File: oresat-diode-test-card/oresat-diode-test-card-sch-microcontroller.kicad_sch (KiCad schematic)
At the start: 25 parts, among them J7 ORESAT-DEBUG-CONNECTOR-ALL, U1 TCAN330, U7 STM32F091C, X2 CRYSTAL-WITH-GND

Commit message: added actual files
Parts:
- removed JP11, JP8: PINHD-2X10, oresat-proto-card:2X10, symbol oresat-proto-card-eagle-import:PINHD-2X10
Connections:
- no-connect marks 6 -> 4

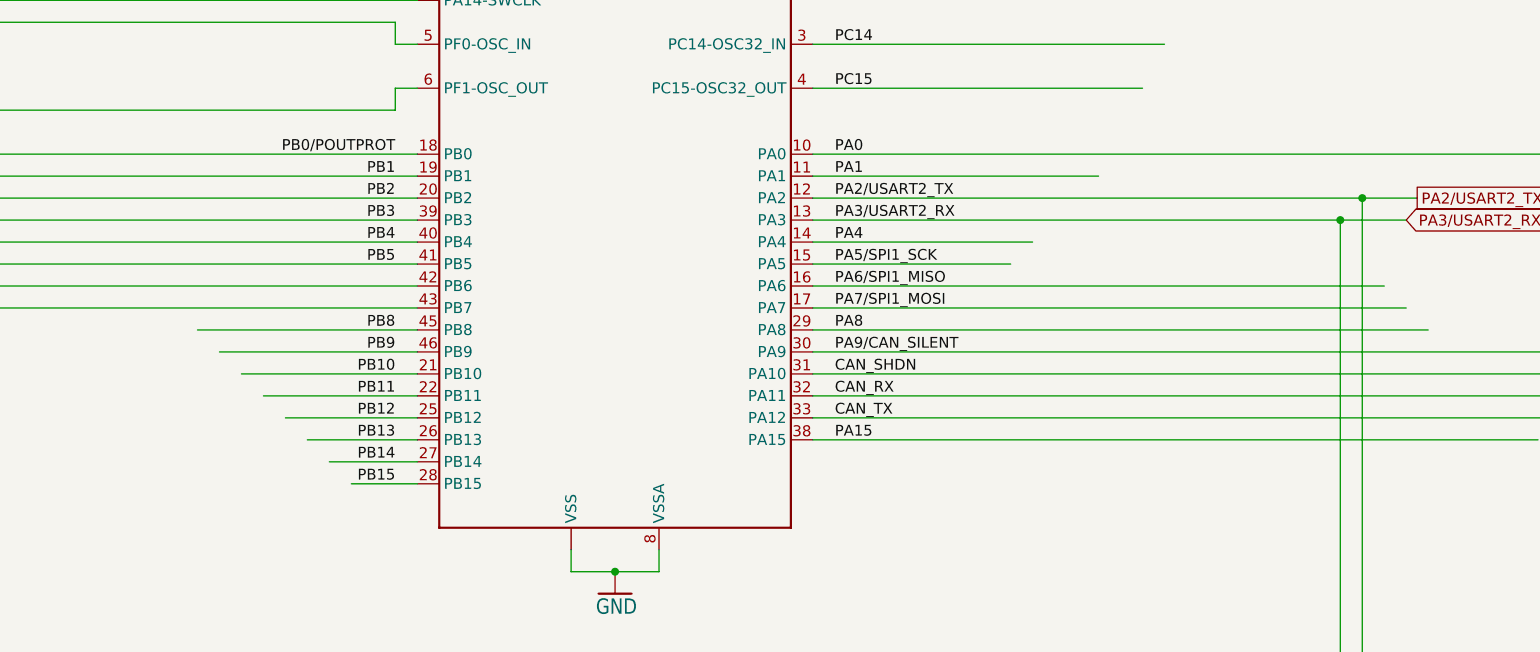
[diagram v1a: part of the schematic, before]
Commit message: Quick design review on schematic; basically ready for layout.
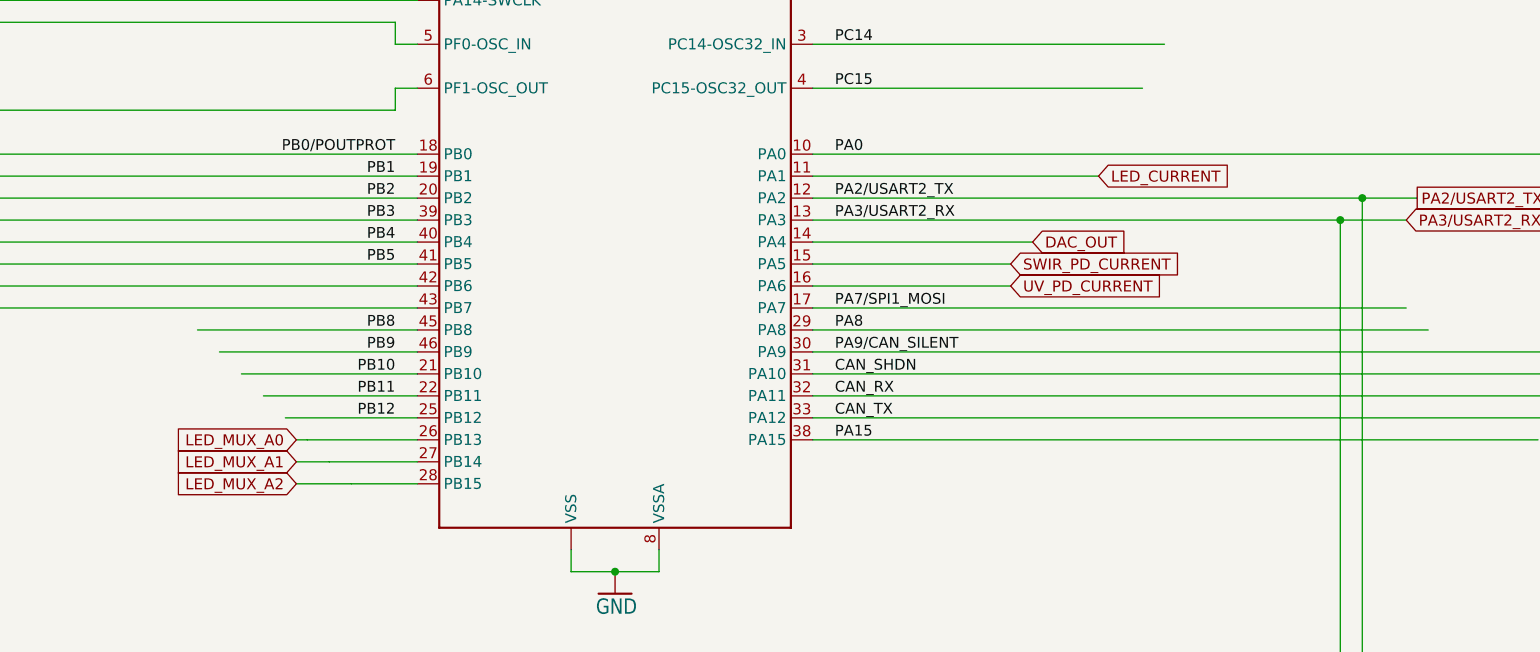
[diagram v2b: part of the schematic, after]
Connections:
- net PA1 renamed LED_CURRENT
- net PA4 renamed DAC_OUT
- net PA5/SPI1_SCK renamed SWIR_PD_CURRENT
- net PA6/SPI1_MISO renamed UV_PD_CURRENT
- net PB13 renamed LED_MUX_A0
- net PB14 renamed LED_MUX_A1
- net PB15 renamed LED_MUX_A2
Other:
- title: OreSat M0 Proto Card: Microcontroller -> OreSat Diode Test Card
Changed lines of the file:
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@@
 	(paper "USLedger")
 	(title_block
-		(title "OreSat M0 Proto Card: Microcontroller")
-		(date "2024-03-21")
-		(rev "5.0")
+		(title "OreSat Diode Test Card")
+		(date "2024-04-21")
+		(rev "v1.0")
 	)
 	(junction
@@
 	(wire
 		(pts
+			(xy 186.69 118.11) (xy 193.04 118.11)
+		)
+		(stroke
+			(width 0)
+			(type default)
+		)
+	)
+	(wire
+		(pts
 			(xy 365.76 102.87) (xy 365.76 107.95)
 		)
@@
 	(wire
 		(pts
+			(xy 186.69 113.03) (xy 187.96 113.03)
+		)
+		(stroke
+			(width 0)
+			(type default)
+		)
+	)
+	(wire
+		(pts
 			(xy 370.84 102.87) (xy 365.76 102.87)
 		)
@@
 	(wire
 		(pts
-			(xy 246.38 95.25) (xy 312.42 95.25)
-		)
-		(stroke
-			(width 0.1524)
-			(type solid)
-		)
-	)
-	(wire
-		(pts
 			(xy 38.1 207.01) (xy 41.91 207.01)
 		)
@@
 	(wire
 		(pts
+			(xy 186.69 115.57) (xy 190.5 115.57)
+		)
+		(stroke
+			(width 0)
+			(type default)
+		)
+	)
+	(wire
+		(pts
 			(xy 215.9 21.59) (xy 220.98 21.59)
 		)
@@
 	(wire
 		(pts
+			(xy 246.38 95.25) (xy 269.24 95.25)
+		)
+		(stroke
+			(width 0)
+			(type default)
+		)
+	)
+	(wire
+		(pts
 			(xy 53.34 214.63) (xy 38.1 214.63)
 		)
@@
 		)
 	)
-	(label "PB14"
-		(at 198.12 115.57 180)
-		(fields_autoplaced yes)
-		(effects
-			(font
-				(size 1.2446 1.2446)
-			)
-			(justify right bottom)
-		)
-	)
 	(label "CAN_SHDN"
 		(at 248.92 105.41 0)
@@
 		)
 	)
-	(label "PB15"
-		(at 198.12 118.11 180)
-		(fields_autoplaced yes)
-		(effects
-			(font
-				(size 1.2446 1.2446)
-			)
-			(justify right bottom)
-		)
-	)
 	(label "NRESET"
 		(at 40.64 171.45 0)
@@
 		)
 	)
-	(label "PA5/SPI1_SCK"
-		(at 248.92 92.71 0)
-		(fields_autoplaced yes)
-		(effects
-			(font
-				(size 1.2446 1.2446)
-			)
-			(justify left bottom)
-		)
-	)
 	(label "PA9/CAN_SILENT"
 		(at 248.92 102.87 0)
@@
 		)
 	)
-	(label "PA1"
-		(at 248.92 82.55 0)
-		(fields_autoplaced yes)
-		(effects
-			(font
-				(size 1.2446 1.2446)
-			)
-			(justify left bottom)
-		)
-	)
-	(label "PA4"
-		(at 248.92 90.17 0)
-		(fields_autoplaced yes)
-		(effects
-			(font
-				(size 1.2446 1.2446)
-			)
-			(justify left bottom)
-		)
-	)
 	(label "BOOT0"
 		(at 198.12 57.15 180)
@@
 		)
 	)
-	(label "PB13"
-		(at 198.12 113.03 180)
-		(fields_autoplaced yes)
-		(effects
-			(font
-				(size 1.2446 1.2446)
-			)
-			(justify right bottom)
-		)
-	)
 	(label "PB2"
 		(at 198.12 85.09 180)
@@
 		)
 	)
-	(label "PA6/SPI1_MISO"
-		(at 248.92 95.25 0)
-		(fields_autoplaced yes)
-		(effects
-			(font
-				(size 1.2446 1.2446)
-			)
-			(justify left bottom)
-		)
-	)
 	(label "PA3/USART2_RX"
 		(at 40.64 186.69 0)
@@
 					(size 1.27 1.27)
 				)
+				(justify right)
+			)
+		)
+	)
+	(global_label "LED_CURRENT"
+		(shape input)
+		(at 279.4 82.55 0)
+		(fields_autoplaced yes)
+		(effects
+			(font
+				(size 1.27 1.27)
+			)
+			(justify left)
+		)
+		(property "Intersheetrefs" "${INTERSHEET_REFS}"
+			(at 295.3875 82.55 0)
+			(effects
+				(font
+					(size 1.27 1.27)
+				)
+				(justify left)
+			)
+		)
+	)
+	(global_label "LED_MUX_A1"
+		(shape input)
+		(at 186.69 115.57 180)
+		(fields_autoplaced yes)
+		(effects
+			(font
+				(size 1.27 1.27)
+			)
+			(justify right)
+		)
+		(property "Intersheetrefs" "${INTERSHEET_REFS}"
+			(at 172.033 115.57 0)
+			(effects
+				(font
+					(size 1.27 1.27)
+				)
+				(justify right)
+			)
+		)
+	)
+	(global_label "DAC_OUT"
+		(shape input)
+		(at 271.78 90.17 0)
+		(fields_autoplaced yes)
+		(effects
+			(font
+				(size 1.27 1.27)
+			)
+			(justify left)
+		)
+		(property "Intersheetrefs" "${INTERSHEET_REFS}"
+			(at 282.99 90.17 0)
+			(effects
+				(font
+					(size 1.27 1.27)
+				)
 				(justify left)
 			)
@@
 		)
 	)
+	(global_label "SWIR_PD_CURRENT"
+		(shape input)
+		(at 269.24 92.71 0)
+		(fields_autoplaced yes)
+		(effects
+			(font
+				(size 1.27 1.27)
+			)
+			(justify left)
+		)
+		(property "Intersheetrefs" "${INTERSHEET_REFS}"
+			(at 289.8237 92.71 0)
+			(effects
+				(font
+					(size 1.27 1.27)
+				)
+				(justify left)
+			)
+		)
+	)
 	(global_label "CAN2_H"
 		(shape bidirectional)
@@
 		)
 	)
+	(global_label "UV_PD_CURRENT"
+		(shape input)
+		(at 269.24 95.25 0)
+		(fields_autoplaced yes)
+		(effects
+			(font
+				(size 1.27 1.27)
+			)
+			(justify left)
+		)
+		(property "Intersheetrefs" "${INTERSHEET_REFS}"
+			(at 287.7071 95.25 0)
+			(effects
+				(font
+					(size 1.27 1.27)
+				)
+				(justify left)
+			)
+		)
+	)
+	(global_label "LED_MUX_A0"
+		(shape input)
+		(at 186.69 113.03 180)
+		(fields_autoplaced yes)
+		(effects
+			(font
+				(size 1.27 1.27)
+			)
+			(justify right)
+		)
+		(property "Intersheetrefs" "${INTERSHEET_REFS}"
+			(at 172.033 113.03 0)
+			(effects
+				(font
+					(size 1.27 1.27)
+				)
+				(justify right)
+			)
+		)
+	)
+	(global_label "LED_MUX_A2"
+		(shape input)
+		(at 186.69 118.11 180)
+		(fields_autoplaced yes)
+		(effects
+			(font
+				(size 1.27 1.27)
+			)
+			(justify right)
+		)
+		(property "Intersheetrefs" "${INTERSHEET_REFS}"
+			(at 172.033 118.11 0)
+			(effects
+				(font
+					(size 1.27 1.27)
+				)
+				(justify right)
+			)
+		)
+	)
 	(global_label "BOOT0"
 		(shape bidirectional)
@@
 			)
 		)
-		(property "Datasheet" ""
+		(property "Datasheet" "https://www.st.com/content/ccc/resource/technical/document/datasheet/95/3c/2e/5b/21/09/45/a6/DM00115237.pdf/files/DM00115237.pdf/jcr:content/translations/en.DM00115237.pdf"
 			(at 223.52 85.09 0)
 			(effects

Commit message: Lots of schematic cleanup - replace weird ground and power symbols with more kicad ones, fix values, fix OPD connections and address, update PCB
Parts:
- removed R50, R51: 4.7k, oresat-passives:0603-C-NOSILK, symbol oresat-proto-card-eagle-import:R-US_0603-C-NOSILK
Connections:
- net PA15: no longer names the net of U7.38 (PA15)
- net PA7/SPI1_MOSI: no longer names the net of U7.17 (PA7)
- net PA8: no longer names the net of U7.29 (PA8)
- net PB1: no longer names the net of U7.19 (PB1)
- net PB10: no longer names the net of U7.21 (PB10)
- net PB11: no longer names the net of U7.22 (PB11)
- net PB12 renamed ~{LED_MUX_ENABLE}
- net PB2: no longer names the net of U7.20 (PB2)
- net PB3: no longer names the net of U7.39 (PB3)
- net PB4: no longer names the net of U7.40 (PB4)
- net PB5: no longer names the net of U7.41 (PB5)
- net PB6/SCL: no longer names the net of U7.42 (PB6)
- net PB7/SDA: no longer names the net of U7.43 (PB7)
- net PB8: no longer names the net of U7.45 (PB8)
- net PB9: no longer names the net of U7.46 (PB9)
- net PC13: no longer names the net of U7.2 (PC13)
- net PC14: no longer names the net of U7.3 (PC14-OSC32_IN)
- net PC15: no longer names the net of U7.4 (PC15-OSC32_OUT)
- no-connect marks 4 -> 21
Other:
- note removed: "Emergency M0 bootstrapping over OPD I2C Address: 0b0111110x"
- moved on the sheet: C13, C14, C15, C18, C19, C20, C21, D5, R47, R48, R49, TP25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

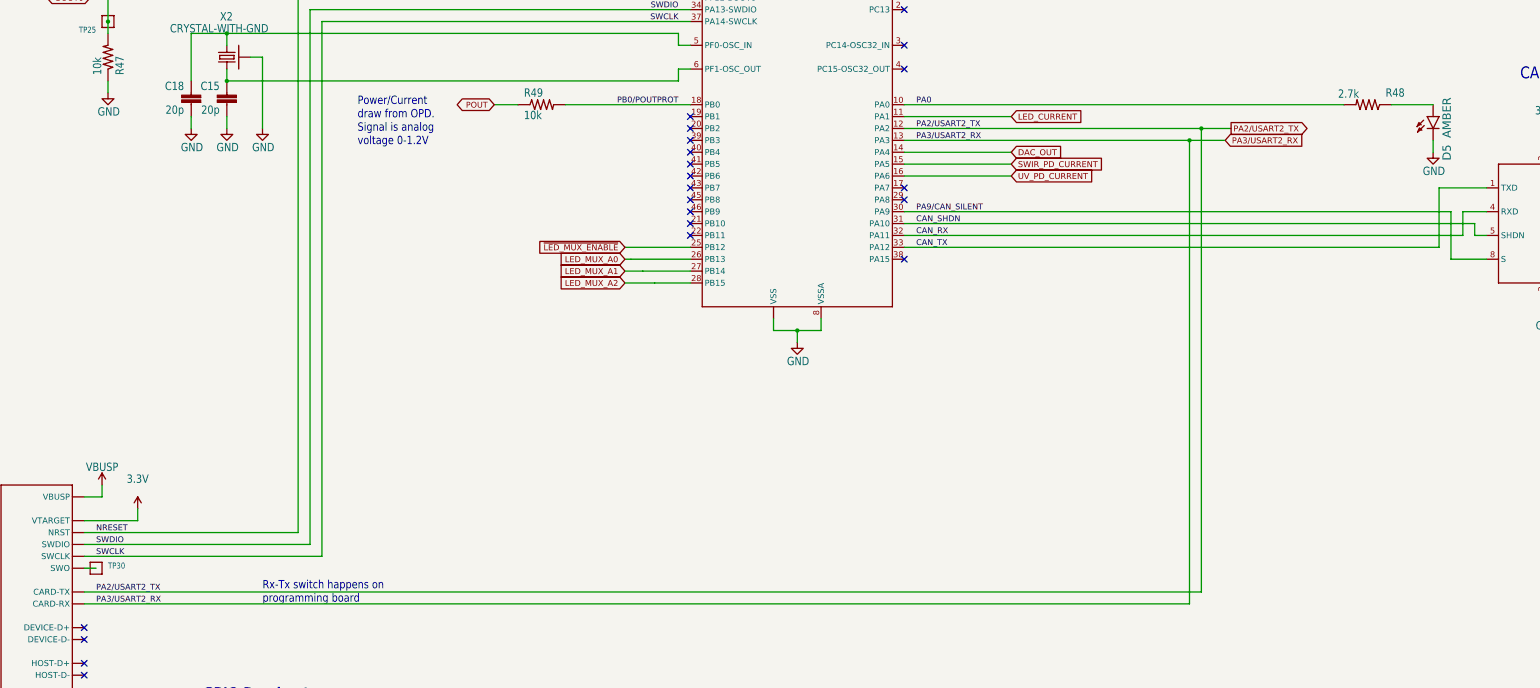
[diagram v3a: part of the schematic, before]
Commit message: Clean up of EAGLE imported ICs, added build directory, moved and locked diode hats.
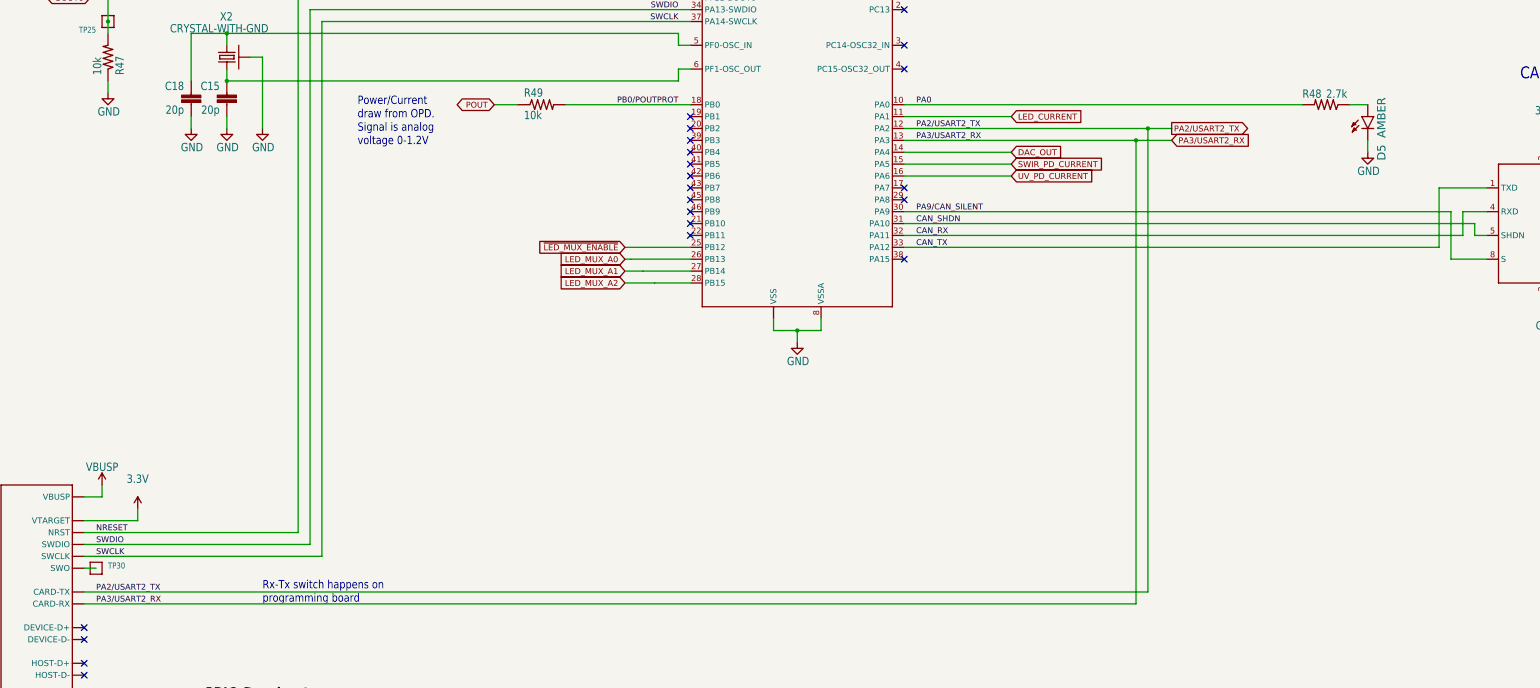
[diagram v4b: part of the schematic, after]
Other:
- moved on the sheet: D5, R48
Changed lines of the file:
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@@
 	)
 	(junction
-		(at 298.45 97.79)
+		(at 287.02 97.79)
 		(diameter 0)
 		(color 0 0 0 0)
 	)
 	(junction
-		(at 300.99 95.25)
+		(at 222.25 31.75)
 		(diameter 0)
 		(color 0 0 0 0)
 	)
 	(junction
-		(at 222.25 31.75)
+		(at 63.5 238.76)
 		(diameter 0)
 		(color 0 0 0 0)
 	)
 	(junction
-		(at 63.5 238.76)
+		(at 212.09 31.75)
 		(diameter 0)
 		(color 0 0 0 0)
 	)
 	(junction
-		(at 212.09 31.75)
+		(at 289.56 95.25)
 		(diameter 0)
 		(color 0 0 0 0)
@@
 	(wire
 		(pts
+			(xy 287.02 97.79) (xy 294.64 97.79)
+		)
+		(stroke
+			(width 0.1524)
+			(type solid)
+		)
+	)
+	(wire
+		(pts
 			(xy 177.8 128.27) (xy 184.15 128.27)
 		)
@@
 	(wire
 		(pts
-			(xy 298.45 196.85) (xy 62.23 196.85)
+			(xy 287.02 196.85) (xy 62.23 196.85)
 		)
 		(stroke
@@
 	(wire
 		(pts
-			(xy 298.45 97.79) (xy 298.45 196.85)
+			(xy 287.02 97.79) (xy 287.02 196.85)
 		)
 		(stroke
@@
 	(wire
 		(pts
-			(xy 237.49 97.79) (xy 298.45 97.79)
-		)
-		(stroke
-			(width 0.1524)
-			(type solid)
-		)
-	)
-	(wire
-		(pts
-			(xy 298.45 97.79) (xy 306.07 97.79)
+			(xy 237.49 97.79) (xy 287.02 97.79)
 		)
 		(stroke
@@
 	(wire
 		(pts
-			(xy 300.99 95.25) (xy 300.99 194.31)
-		)
-		(stroke
-			(width 0.1524)
-			(type solid)
-		)
-	)
-	(wire
-		(pts
-			(xy 300.99 95.25) (xy 307.34 95.25)
+			(xy 289.56 95.25) (xy 289.56 194.31)
 		)
 		(stroke
@@
 	(wire
 		(pts
-			(xy 237.49 90.17) (xy 331.47 90.17)
+			(xy 237.49 90.17) (xy 322.58 90.17)
 		)
 		(stroke
@@
 	(wire
 		(pts
-			(xy 237.49 95.25) (xy 300.99 95.25)
+			(xy 237.49 95.25) (xy 289.56 95.25)
 		)
 		(stroke
@@
 	(wire
 		(pts
-			(xy 350.52 97.79) (xy 350.52 100.33)
+			(xy 336.55 97.79) (xy 336.55 100.33)
 		)
 		(stroke
@@
 	(wire
 		(pts
-			(xy 300.99 194.31) (xy 62.23 194.31)
+			(xy 289.56 194.31) (xy 62.23 194.31)
 		)
 		(stroke
@@
 	(wire
 		(pts
+			(xy 289.56 95.25) (xy 294.64 95.25)
+		)
+		(stroke
+			(width 0.1524)
+			(type solid)
+		)
+	)
+	(wire
+		(pts
 			(xy 222.25 31.75) (xy 227.33 31.75)
 		)
@@
 	(wire
 		(pts
-			(xy 341.63 90.17) (xy 350.52 90.17)
+			(xy 332.74 90.17) (xy 336.55 90.17)
 		)
 		(stroke
@@
 	(global_label "PA2{slash}USART2_TX"
 		(shape output)
-		(at 307.34 95.25 0)
+		(at 294.64 95.25 0)
 		(fields_autoplaced yes)
 		(effects
@@
 		)
 		(property "Intersheetrefs" "${INTERSHEET_REFS}"
-			(at 325.3648 95.25 0)
+			(at 312.6648 95.25 0)
 			(effects
 				(font
@@
 		)
 	)
-	(global_label "PA3{slash}USART2_RX"
+	(global_label "LED_CURRENT"
 		(shape input)
-		(at 306.07 97.79 0)
+		(at 260.35 92.71 0)
+		(fields_autoplaced yes)
 		(effects
 			(font
@@
 		)
 		(property "Intersheetrefs" "${INTERSHEET_REFS}"
-			(at 307.3945 97.7106 0)
+			(at 276.3375 92.71 0)
 			(effects
 				(font
 					(size 1.27 1.27)
 				)
-				(justify right)
+				(justify left)
 			)
 		)
 	)
-	(global_label "LED_CURRENT"
+	(global_label "~{LED_MUX_ENABLE}"
 		(shape input)
-		(at 260.35 92.71 0)
+		(at 177.8 120.65 180)
 		(fields_autoplaced yes)
 		(effects
@@
 				(size 1.27 1.27)
 			)
-			(justify left)
+			(justify right)
 		)
 		(property "Intersheetrefs" "${INTERSHEET_REFS}"
-			(at 276.3375 92.71 0)
+			(at 158.4259 120.65 0)
 			(effects
 				(font
 					(size 1.27 1.27)
 				)
-				(justify left)
+				(justify right)
 			)
 		)
 	)
-	(global_label "~{LED_MUX_ENABLE}"
+	(global_label "PA3{slash}USART2_RX"
 		(shape input)
-		(at 177.8 120.65 180)
+		(at 294.64 97.79 0)
 		(fields_autoplaced yes)
 		(effects
@@
 				(size 1.27 1.27)
 			)
-			(justify right)
+			(justify left)
 		)
 		(property "Intersheetrefs" "${INTERSHEET_REFS}"
-			(at 158.4259 120.65 0)
+			(at 313.0466 97.79 0)
 			(effects
 				(font
 					(size 1.27 1.27)
 				)
-				(justify right)
+				(justify left)
 			)
 		)
@@
 	(symbol
 		(lib_id "oresat-proto-card-eagle-import:R-US_0603-C-NOSILK")
-		(at 336.55 90.17 180)
+		(at 327.66 90.17 180)
 		(unit 1)
 		(exclude_from_sim no)
@@
 		(dnp no)
 		(property "Reference" "R48"
-			(at 340.36 88.6714 0)
+			(at 322.58 88.9 0)
 			(effects
 				(font
@@
 		)
 		(property "Value" "2.7k"
-			(at 330.2 88.9 0)
+			(at 327.66 88.9 0)
 			(effects
 				(font
@@
 		)
 		(property "Footprint" "oresat-passives:0603-C-NOSILK"
-			(at 336.55 90.17 0)
+			(at 327.66 90.17 0)
 			(effects
 				(font
@@
 		)
 		(property "Datasheet" ""
-			(at 336.55 90.17 0)
+			(at 327.66 90.17 0)
 			(effects
 				(font
@@
 		)
 		(property "Description" ""
-			(at 336.55 90.17 0)
+			(at 327.66 90.17 0)
 			(effects
 				(font
@@
 		)
 		(property "DIS" "Digi-Key"
-			(at 336.55 90.17 0)
+			(at 327.66 90.17 0)
 			(effects
 				(font
@@
 		)
 		(property "DPN" "A129632CT-ND"
-			(at 336.55 90.17 0)
+			(at 327.66 90.17 0)
 			(effects
 				(font
@@
 		)
 		(property "MFR" "TE Connectivity"
-			(at 336.55 90.17 0)
+			(at 327.66 90.17 0)
 			(effects
 				(font
@@
 		)
 		(property "MPN" "CRGCQ0402F2K7"
-			(at 336.55 90.17 0)
+			(at 327.66 90.17 0)
 			(effects
 				(font
@@
 	(symbol
 		(lib_id "oresat-proto-card-eagle-import:LED-GREEN0603")
-		(at 350.52 92.71 0)
+		(at 336.55 92.71 0)
 		(unit 1)
 		(exclude_from_sim no)
@@
 		(dnp no)
 		(property "Reference" "D5"
-			(at 352.425 102.108 90)
+			(at 338.455 102.108 90)
 			(effects
 				(font
@@
 		)
 		(property "Value" "AMBER"
-			(at 352.425 97.282 90)
+			(at 338.455 97.282 90)
 			(effects
 				(font
@@
 		)
 		(property "Footprint" "oresat-proto-card:LED-0603"
-			(at 350.52 92.71 0)
+			(at 336.55 92.71 0)
 			(effects
 				(font
@@
 		)
 		(property "Datasheet" ""
-			(at 350.52 92.71 0)
+			(at 336.55 92.71 0)
 			(effects
 				(font
@@
 		)
 		(property "Description" ""
-			(at 350.52 92.71 0)
+			(at 336.55 92.71 0)
 			(effects
 				(font
@@
 		)
 		(property "DIS" "Digi-Key"
-			(at 350.52 92.71 0)
+			(at 336.55 92.71 0)
 			(effects
 				(font
@@
 		)
 		(property "DPN" "1830-1064-1-ND"
-			(at 350.52 92.71 0)
+			(at 336.55 92.71 0)
 			(effects
 				(font
@@
 		)
 		(property "MFR" "Inolux"
-			(at 350.52 92.71 0)
+			(at 336.55 92.71 0)
 			(effects
 				(font
@@
 		)
 		(property "MPN" "IN-S63AT5A"
-			(at 350.52 92.71 0)
+			(at 336.55 92.71 0)
 			(effects
 				(font
@@
 	(symbol
 		(lib_id "power:GND")
-		(at 350.52 100.33 0)
+		(at 336.55 100.33 0)
 		(mirror y)
 		(unit 1)
@@
 		(dnp no)
 		(property "Reference" "#GND062"
-			(at 350.52 100.33 0)
+			(at 336.55 100.33 0)
 			(effects
 				(font
@@
 		)
 		(property "Value" "GND"
-			(at 353.06 105.41 0)
+			(at 339.09 105.41 0)
 			(effects
 				(font
@@
 		)
 		(property "Footprint" ""
-			(at 350.52 100.33 0)
+			(at 336.55 100.33 0)
 			(effects
 				(font
@@
 		)
 		(property "Datasheet" ""
-			(at 350.52 100.33 0)
+			(at 336.55 100.33 0)
 			(effects
 				(font
@@
 		)
 		(property "Description" "Power symbol creates a global label with name \"GND\" , ground"
-			(at 350.52 100.33 0)
+			(at 336.55 100.33 0)
 			(effects
 				(font
